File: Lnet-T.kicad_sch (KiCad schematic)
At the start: 8 parts, among them J501 RJ12, J502 RJ12, U501 LM311

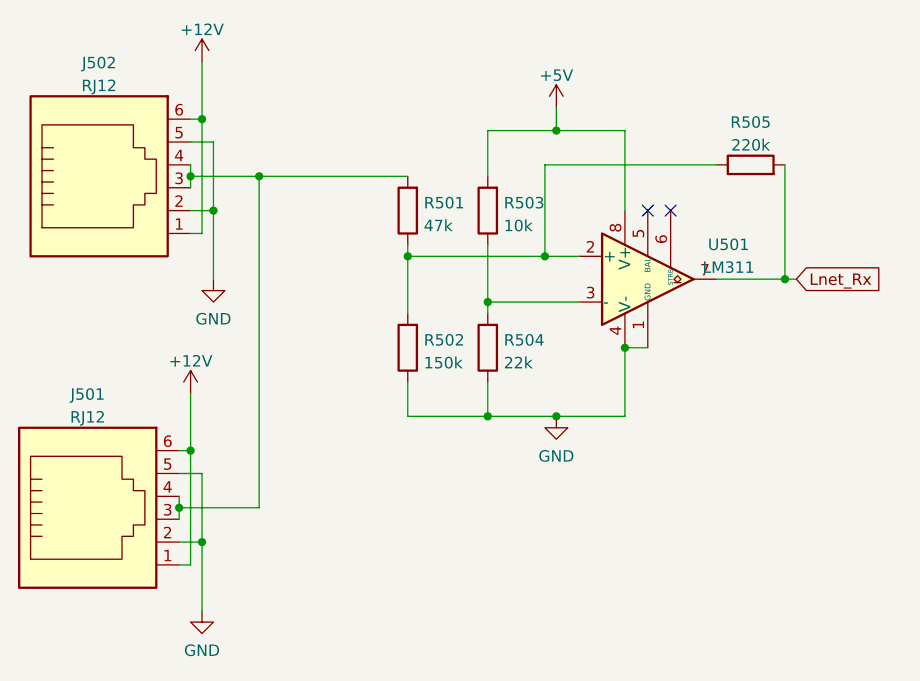
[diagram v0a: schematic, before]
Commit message: added hierarchial labels to some schematics
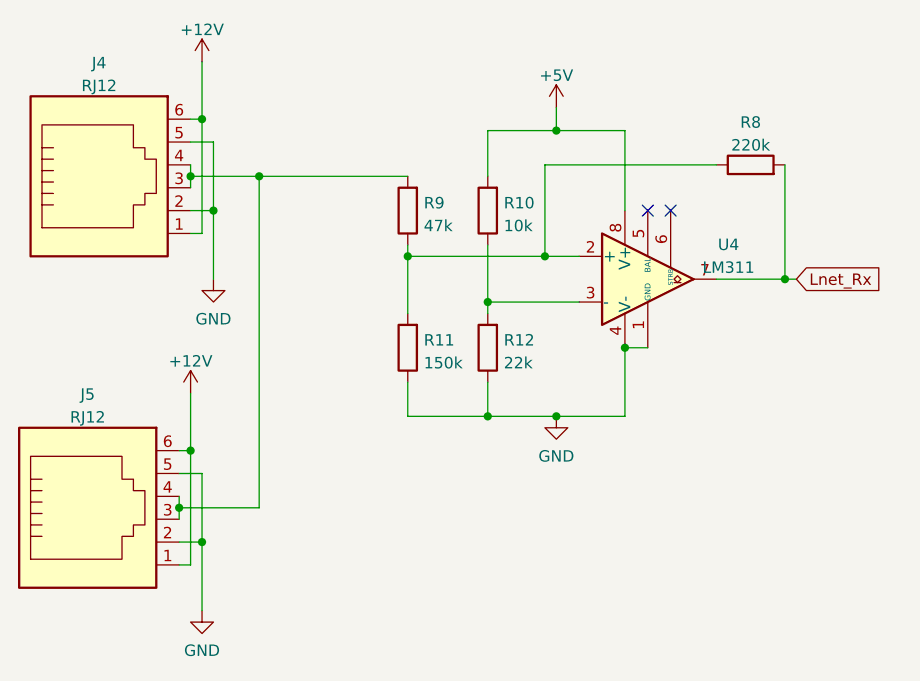
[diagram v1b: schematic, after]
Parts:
- renumbered J502 to J4, J501 to J5, R503 to R10, R502 to R11, R504 to R12, R505 to R8, R501 to R9, U501 to U4
